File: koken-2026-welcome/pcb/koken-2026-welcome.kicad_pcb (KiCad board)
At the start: 2 copper layers, 44 x 44 mm, 24 parts, among them J1 USB_C_Receptacle_USB2.0_16P, J2 Conn_01x03_Pin, SW1 SW_Push, SW2 SW_SPDT, U1 CH32V003JxMx, U2 AP7333

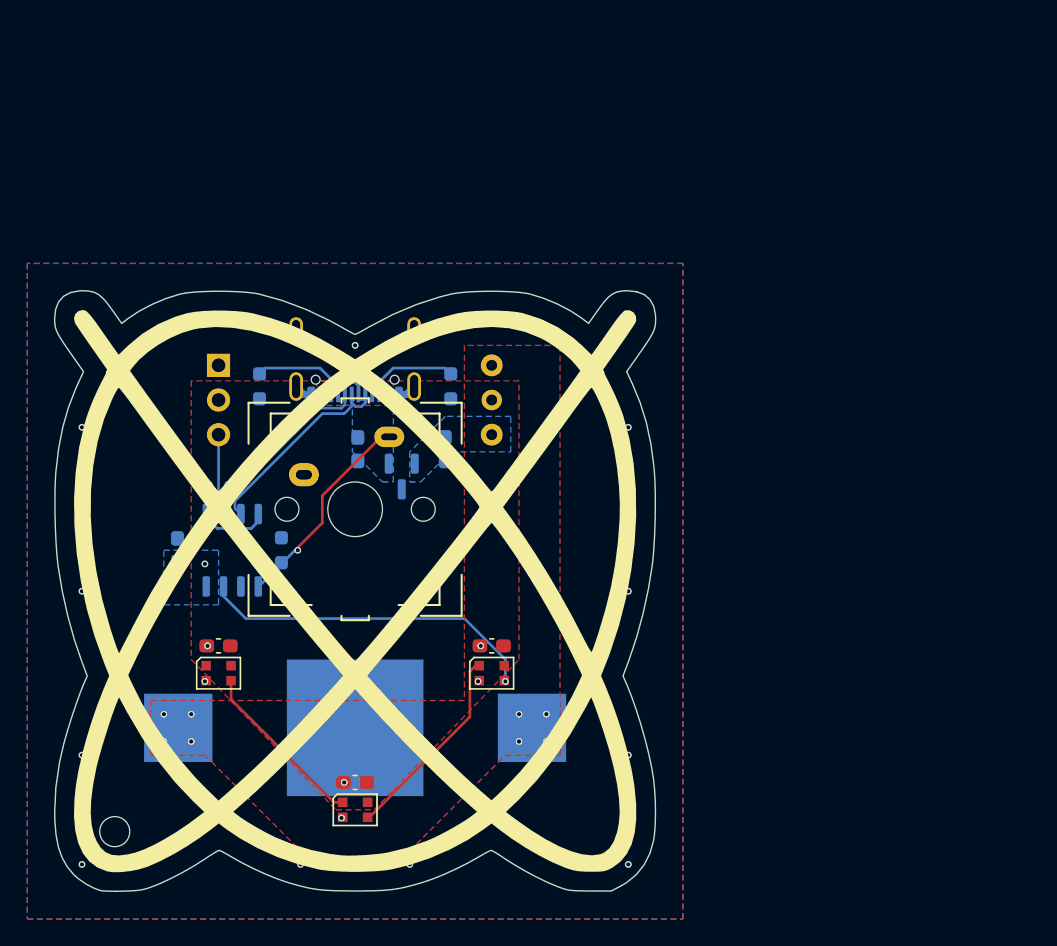
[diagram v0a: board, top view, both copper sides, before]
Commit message: koken-2026-welcome 新しい基板の配線を設計
キースイッチをkailhに
ws2812を2個に
ldoを変更
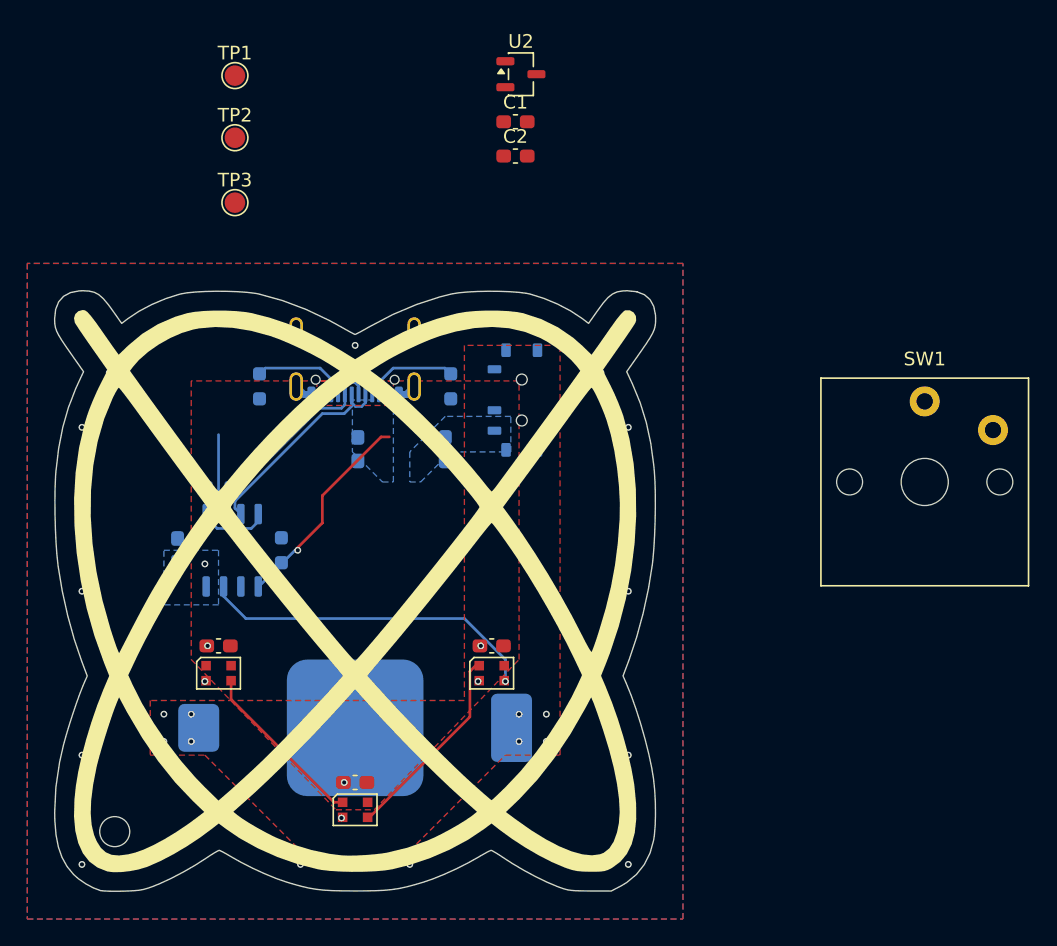
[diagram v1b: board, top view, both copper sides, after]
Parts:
- removed J2: Conn_01x03_Pin, Connector_PinHeader_2.54mm:PinHeader_1x03_P2.54mm_Vertical
- added C1: 1u, Capacitor_SMD:C_0603_1608Metric_Pad1.08x0.95mm_HandSolder, F.Cu at (111.7, 65.6)
- added C2: 1u, Capacitor_SMD:C_0603_1608Metric_Pad1.08x0.95mm_HandSolder, F.Cu at (111.7, 68.1)
- added TP1: VDD, TestPoint:TestPoint_Pad_D1.5mm, F.Cu at (91.2, 62.2)
- added TP2: GND, TestPoint:TestPoint_Pad_D1.5mm, F.Cu at (91.2, 66.8)
- added TP3: SWIO, TestPoint:TestPoint_Pad_D1.5mm, F.Cu at (91.2, 71.5)
- BT1: value CR2032 -> CR2032(MY-2032-10); footprint Battery:BatteryHolder_Multicomp_BC-2001_1x2032 -> Library:MY-2032-10
- SW1: value SW_Push -> kailh low profile key switch; footprint Library:CherryMX_Red -> Library:SW_Kailh_Choc_V1
- SW2: value SW_SPDT -> MSK12C02G25-B; footprint Button_Switch_THT:SW_Slide-03_Wuerth-WS-SLTV_10x2.5x6.4_P2.54mm -> Library:MSK12C02G25-B
- U1: value CH32V003JxMx -> CH32V003J4M6
- U2: value AP7333 -> XC6206P332MR; footprint Library:AP7333 -> Package_TO_SOT_SMD:SOT-23-3; moved to F.Cu
- moved SW1 41.7 mm to (141.7, 92.0)
- moved U2 31.2 mm to (112.1, 62.1), turned to 0 degrees
- moved BT1 11.5 mm to (88.5, 110.0)
- moved SW2 2.20 mm to (112.2, 86.0)
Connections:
- D2 pad 1: Net-(D2-DOUT) -> unconnected-(D2-DOUT-Pad1)
- SW1 pad 1: VDD -> KEY
- SW1 pad 2: KEY -> GND
- U2 pad 1: +5V -> GND
- U2 pad 3: GND -> +5V

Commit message: 基板試作2号
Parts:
- removed the C1 at (111.7, 65.6)
- removed the C1 at (100.2, 89.6)
- removed the C2 at (111.7, 68.1)
- removed the C2 at (106.6, 89.6)
- removed C5: 100n, Capacitor_SMD:C_0603_1608Metric_Pad1.08x0.95mm_HandSolder
- removed D3: WS2812B-2020, LED_SMD:LED_WS2812B-2020_PLCC4_2.0x2.0mm
- removed R4: 10k, Resistor_SMD:R_0603_1608Metric_Pad0.98x0.95mm_HandSolder
- added C1: 1u, Capacitor_SMD:C_0603_1608Metric_Pad1.08x0.95mm_HandSolder, F.Cu at (108.9, 85.2)
- added C2: 1u, Capacitor_SMD:C_0603_1608Metric_Pad1.08x0.95mm_HandSolder, F.Cu at (105.1, 87.5)
- ?: value https://ueckoken.club/ -> ueckoken.club
- C6, H1, J1, R1, R2, R3, SW2, U1: moved to F.Cu
- TP1, TP2, TP3: moved to B.Cu
- moved SW1 42.7 mm to (100.0, 101.0)
- moved TP1 38.1 mm to (111.9, 94.2), turned to -90 degrees
- moved TP2 35.9 mm to (114.5, 94.2), turned to -90 degrees
- moved TP3 34.3 mm to (117.0, 94.2), turned to -90 degrees
- moved H1 34.2 mm to (83.0, 83.4), turned to 0 degrees
- moved C6 31.8 mm to (116.8, 85.7), turned to 180 degrees
- moved ? 26.9 mm to (93.5, 89.3)
- moved U2 25.8 mm to (108.9, 87.7), turned to 180 degrees
- moved U1 25.0 mm to (114.8, 89.3), turned to 180 degrees
- moved R3 23.7 mm to (112.8, 85.7), turned to 180 degrees
- moved BT1 23.2 mm to (111.5, 113.6), turned to 180 degrees
- moved D2 14.1 mm to (90.1, 105.9)
- moved R1 13.1 mm to (106.1, 85.0)
- moved R2 13.1 mm to (93.9, 85.0)
- moved C4 11.5 mm to (109.8, 108.0), turned to 0 degrees
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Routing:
- net VDD: track 0.31 -> 58.7 mm, vias 1 -> 2
- net BAT: track 0.00 -> 56.2 mm, vias 8 -> 1
- net +5V: track 0.00 -> 15.6 mm, vias 4 -> 0
- net Net-(D2-DOUT): track 12.7 -> 0.00 mm
- net SWIO: track 10.8 -> 6.12 mm, vias 0 -> 1
- net +3.3V: track 0.00 -> 4.46 mm
- net D-: track 15.8 -> 19.9 mm
- net KEY: track 15.5 -> 19.3 mm, vias 1 -> 0
- net Net-(D1-DOUT): track 14.9 -> 18.2 mm
- net WS2812C: track 24.9 -> 21.9 mm, vias 1 -> 0
- net D+: track 15.2 -> 16.6 mm
- net GND: track 2.72 -> 3.25 mm, vias 43 -> 40
- net Net-(J1-CC1): track 7.08 -> 7.19 mm, vias 0 -> 2
- removed copper zone on B.Cu, net +3.3V
- removed copper zone on B.Cu, net +5V
- removed copper zone on F.Cu, net +5V
- removed copper zone on F.Cu, net BAT
- removed copper zone on B.Cu, net VDD
- removed copper zone on F.Cu, net VDD
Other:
- board text removed: "0u1"
- board text removed: "10k"
- board text removed: "1k5"
- board text removed: "1u"
- board text removed: "3V3"
- board text removed: "4k7"
- board text removed: "AP7333"
- board text removed: "BAT"
- board text removed: "GND"
- board text removed: "SWIO"
- board text removed: "VDD"
- board text removed: "ueckoken.club"
